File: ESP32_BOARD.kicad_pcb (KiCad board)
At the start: 4 copper layers, 36 x 70 mm, 70 parts, among them IC1 AP2112K-3.3, IC2 MPQ4420HGJ-Z, IC3 W25Q128JVSIQ, IC4 ESP32-S3R8, IC5 AW9364DNR, Q1 40MHz, SW1 TS-1010B-B-A, SW2 PTS810SJK250SMTRLFS, SW3 PTS810SJK250SMTRLFS

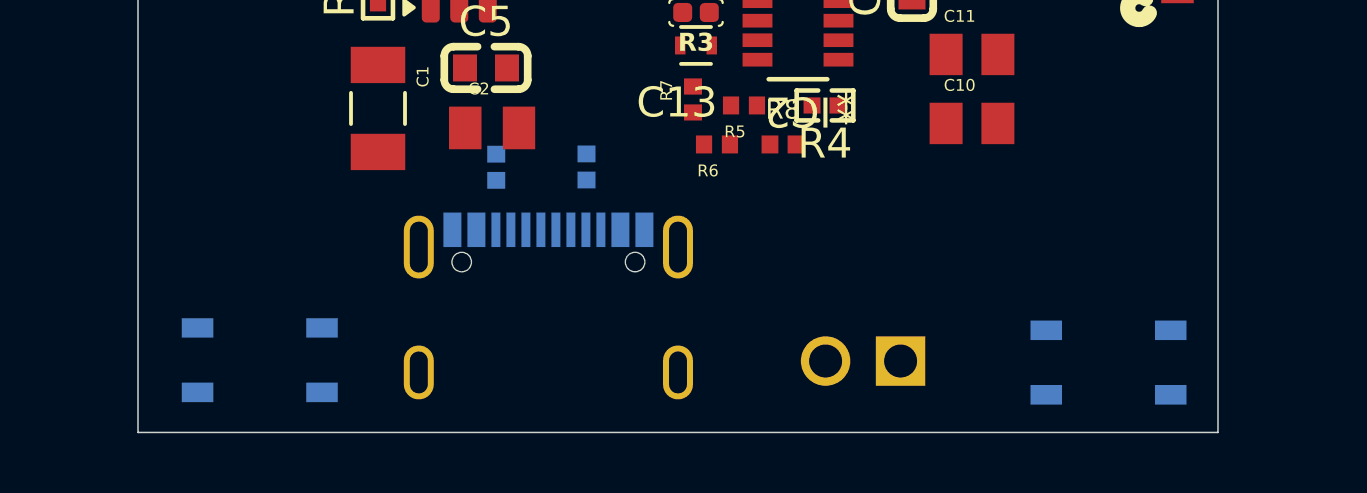
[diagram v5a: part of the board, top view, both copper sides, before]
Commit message: Origin of PCB Layout changed
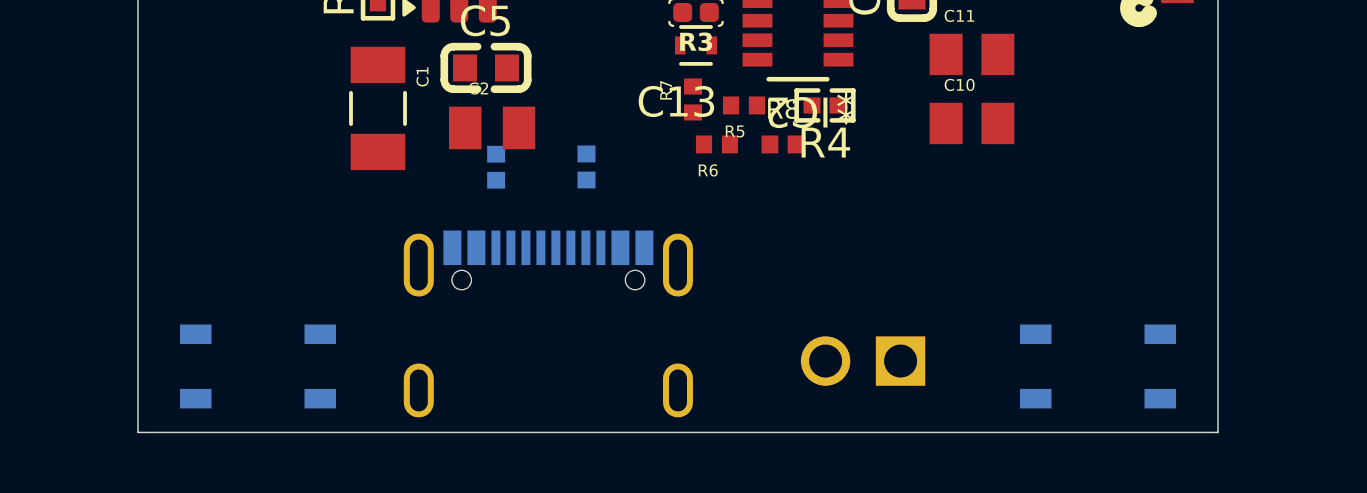
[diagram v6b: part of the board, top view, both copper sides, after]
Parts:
- moved ST2 0.60 mm to (91.1, 152.8)
- moved SW2 0.37 mm to (109.4, 152.0)
- moved SW3 0.22 mm to (81.4, 152.0)
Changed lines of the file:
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@@
 		(allow_soldermask_bridges_in_footprints no)
 		(tenting front back)
+		(aux_axis_origin 77.4 154.2)
 		(grid_origin 77.4 154.2)
 		(pcbplotparams
@@
 	(footprint "PTS810SJK250SMTRLFS:PTS810SJG250SMTRLFS"
 		(layer "B.Cu")
-		(at 109.75 151.87 180)
+		(at 109.4 152 180)
 		(descr "<b>pts810</b><br>")
 		(property "Reference" "SW2"
@@
 	(footprint "PTS810SJK250SMTRLFS:PTS810SJG250SMTRLFS"
 		(layer "B.Cu")
-		(at 81.46 151.79)
+		(at 81.4 152)
 		(descr "<b>pts810</b><br>")
 		(property "Reference" "SW3"
@@
 	(footprint "TYPE-C-USB4105-GF-A:GCT_USB4105-GF-A"
 		(layer "B.Cu")
-		(at 91.08 152.2 180)
+		(at 91.08 152.8 180)
 		(property "Reference" "ST2"
 			(at 6.775 8.435 0)
@@
 		(layer "Edge.Cuts")
 	)
+	(dimension
+		(type orthogonal)
+		(layer "Dwgs.User")
+		(pts
+			(xy 77.4 154.2) (xy 113.4 154.2)
+		)
+		(height 5.32)
+		(orientation 0)
+		(format
+			(prefix "")
+			(suffix "")
+			(units 2)
+			(units_format 0)
+			(precision 4)
+			(suppress_zeroes yes)
+		)
+		(style
+			(thickness 0.1)
+			(arrow_length 1.27)
+			(text_position_mode 0)
+			(arrow_direction outward)
+			(extension_height 0.58642)
+			(extension_offset 0.5)
+			(keep_text_aligned yes)
+		)
+		(gr_text "36"
+			(at 95.4 158.37 0)
+			(layer "Dwgs.User")
+			(effects
+				(font
+					(size 1 1)
+					(thickness 0.15)
+				)
+			)
+		)
+	)
+	(dimension
+		(type orthogonal)
+		(layer "Dwgs.User")
+		(pts
+			(xy 77.4 154.2) (xy 77.4 84.2)
+		)
+		(height -4.02)
+		(orientation 1)
+		(format
+			(prefix "")
+			(suffix "")
+			(units 3)
+			(units_format 0)
+			(precision 4)
+			(suppress_zeroes yes)
+		)
+		(style
+			(thickness 0.1)
+			(arrow_length 1.27)
+			(text_position_mode 0)
+			(arrow_direction outward)
+			(extension_height 0.58642)
+			(extension_offset 0.5)
+			(keep_text_aligned yes)
+		)
+		(gr_text "70"
+			(at 72.23 119.2 90)
+			(layer "Dwgs.User")
+			(effects
+				(font
+					(size 1 1)
+					(thickness 0.15)
+				)
+			)
+		)
+	)
 	(embedded_fonts no)

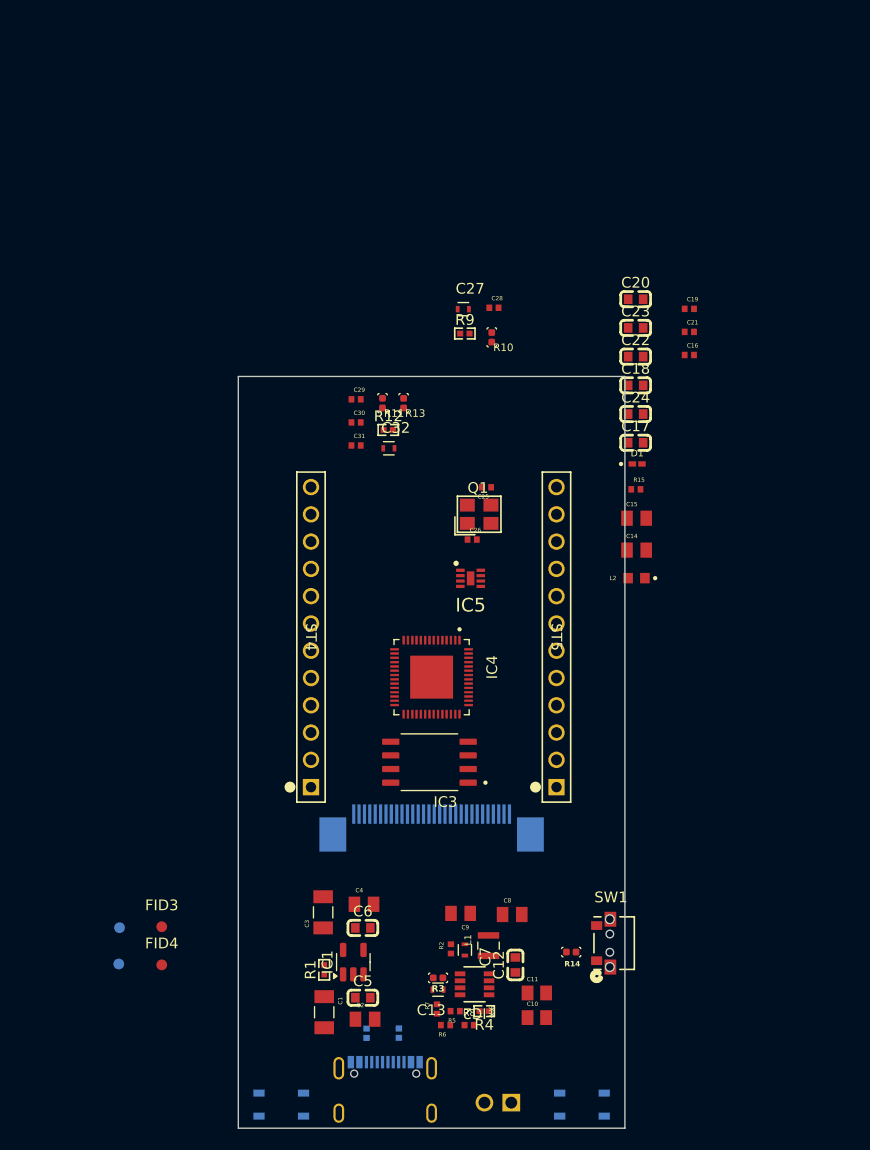
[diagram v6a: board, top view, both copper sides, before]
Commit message: Lazy Layout Done
Needed additional movement of the components to achieve better routing
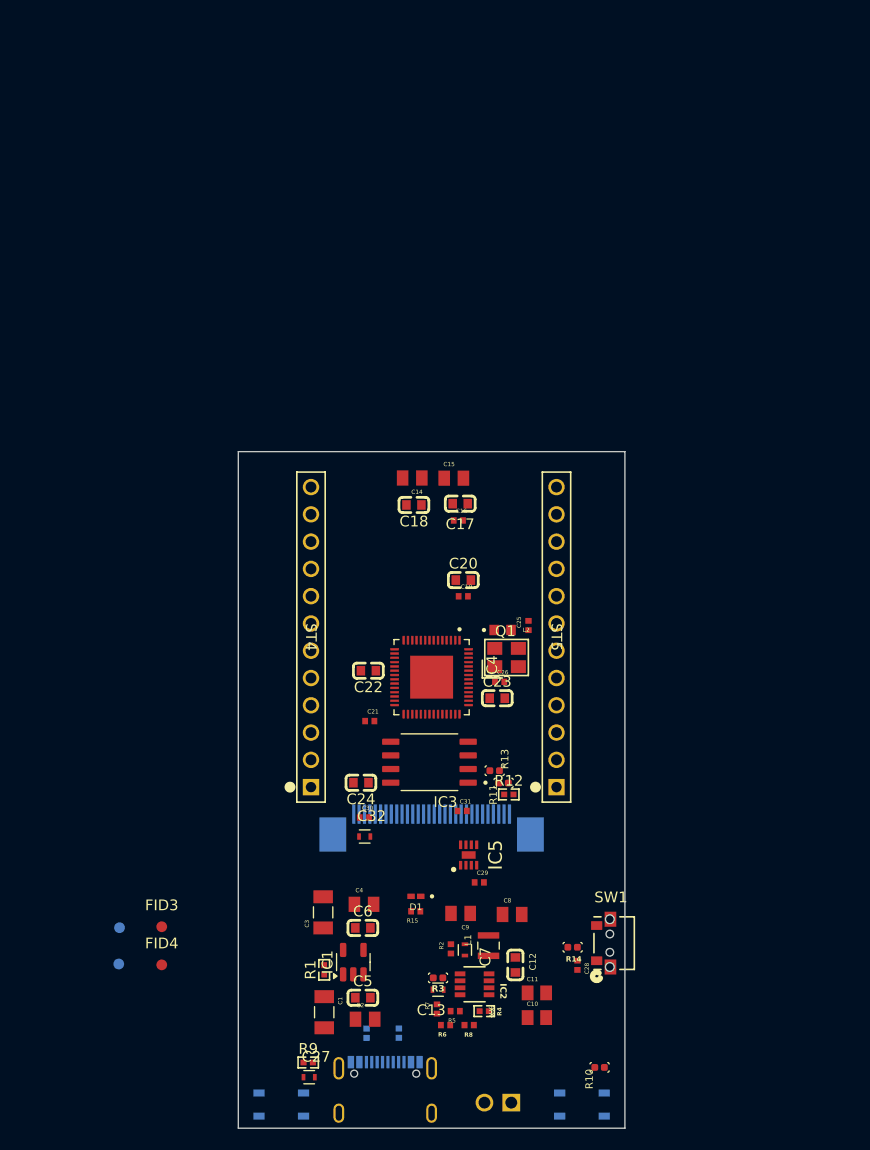
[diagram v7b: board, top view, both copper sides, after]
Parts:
- moved C27 72.9 mm to (84.0, 149.4)
- moved R9 69.4 mm to (83.9, 148.1)
- moved R10 68.7 mm to (111.0, 148.5), turned to -90 degrees
- moved C28 61.7 mm to (109.0, 139.0), turned to -90 degrees
- moved C21 46.9 mm to (89.6, 116.3)
- moved C29 46.4 mm to (99.8, 131.3)
- moved D1 45.2 mm to (93.9, 132.6), turned to 180 degrees
- moved R15 44.3 mm to (93.9, 134.0), turned to 180 degrees
- moved C24 42.8 mm to (88.8, 122.0), turned to 180 degrees
- moved C22 38.4 mm to (89.5, 111.6), turned to 180 degrees
- moved R11 37.1 mm to (102.1, 122.1), turned to -90 degrees
- moved C23 36.8 mm to (101.5, 114.2)
- moved C30 36.8 mm to (89.1, 125.3)
- moved C32 36.2 mm to (89.2, 127.0)
- moved R12 35.7 mm to (102.6, 123.1)
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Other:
- board size 36 x 70 mm -> 36 x 63 mm

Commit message: Most of the layout done
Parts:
- moved R9 11.6 mm to (79.8, 137.3)
- moved R10 10.2 mm to (106.9, 139.2)
- moved C2 5.85 mm to (83.7, 142.2), turned to 180 degrees
- moved C15 5.11 mm to (99.4, 98.4)
- moved C14 5.11 mm to (95.5, 98.4)
- moved Q1 4.77 mm to (104.7, 106.2), turned to 90 degrees
- moved C26 4.76 mm to (104.7, 108.9), turned to 180 degrees
- moved C3 4.75 mm to (90.0, 133.4), turned to 0 degrees
- moved C18 4.63 mm to (96.1, 100.2)
- moved C4 4.32 mm to (84.8, 133.4), turned to 180 degrees
- moved C16 4.31 mm to (96.3, 101.6), turned to 180 degrees
- moved IC4 4.27 mm to (95.3, 107.9)
- moved C17 4.24 mm to (99.0, 100.2)
- moved C27 4.16 mm to (79.8, 149.1)
- moved C23 4.13 mm to (101.2, 110.0), turned to -90 degrees
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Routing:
- net GND: track 0.00 -> 108.8 mm, vias 0 -> 81
- net BOOT: track 0.00 -> 55.5 mm, vias 0 -> 1
- net I2C_SDA: track 0.00 -> 24.5 mm, vias 0 -> 1
- net I2C_SCL: track 0.00 -> 20.5 mm, vias 0 -> 1
- net ESP_TP_RESET: track 0.00 -> 18.4 mm
- net GPIO1: track 0.00 -> 17.1 mm
- net GPIO0: track 0.00 -> 16.6 mm, vias 0 -> 1
- net +3V3: track 0.00 -> 16.1 mm, vias 0 -> 23
- net ESP_TP_INT: track 0.00 -> 15.5 mm, vias 0 -> 1
- net GPIO2: track 0.00 -> 15.4 mm
- net GPIO3: track 0.00 -> 14.7 mm
- net GPIO13: track 0.00 -> 12.3 mm
- net GPIO12: track 0.00 -> 10.7 mm
- net GPIO11: track 0.00 -> 9.86 mm
- net GPIO10: track 0.00 -> 9.39 mm
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- added copper zone on F.Cu, net +12V
- added copper zone on In2.Cu, net +12V
- added copper zone on F.Cu, net +3V3
- added copper zone on In2.Cu, net +3V3
- added copper zone on F.Cu, net +5V
- added copper zone on In2.Cu, net +5V
- added copper zone on In1.Cu, net GND
